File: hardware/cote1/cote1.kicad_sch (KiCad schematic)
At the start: 0 parts

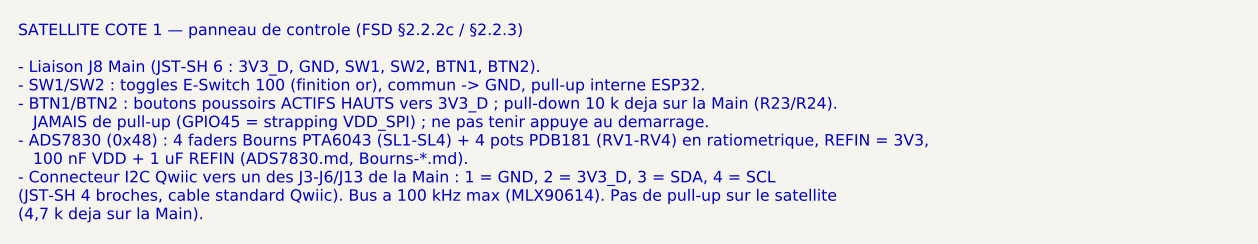
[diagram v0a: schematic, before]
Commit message: hardware+docs: CAP1298 retenu pour le tactile de Cote 2, BOM de reference corrigee (H8)
- Cote 2 : CAP1298-1-SL-TR (C2652072, 8 touches, 0x28 fixe) remplace le MTCH2120
  (aucun stock) ; proximite de Cote 3 en suspens (pas de second CAP12xx).
- BOM : U11 = LSM6DSOXTR, doublon U21 retire, filtre DAC 470 ohm + 2,2 nF C0G,
  TMAG5273A1 (C3716049), U10 SOT-23-6, ecran bouche a choisir, LCSC de D1/Q1/Q2
  dans la bonne colonne, ST25DV et haut-parleur ajoutes.
- docs/pcb/02-bom-lcsc.csv (perimee) supprimee : une seule BOM.
- FSD, RESTE-A-FAIRE, syntheses et cartouches satellites alignes.
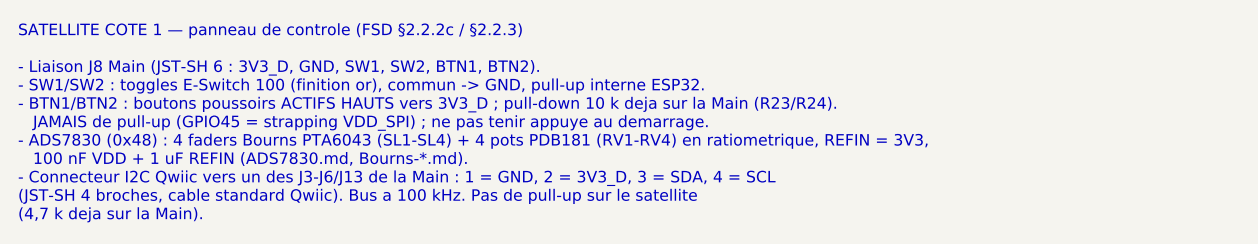
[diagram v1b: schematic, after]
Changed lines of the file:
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@@
 	(generator_version "10.0")
 	(paper "A4")
-	(text "SATELLITE COTE 1 — panneau de controle (FSD §2.2.2c / §2.2.3)\n\n- Liaison J8 Main (JST-SH 6 : 3V3_D, GND, SW1, SW2, BTN1, BTN2).\n- SW1/SW2 : toggles E-Switch 100 (finition or), commun -> GND, pull-up interne ESP32.\n- BTN1/BTN2 : boutons poussoirs ACTIFS HAUTS vers 3V3_D ; pull-down 10 k deja sur la Main (R23/R24).\n   JAMAIS de pull-up (GPIO45 = strapping VDD_SPI) ; ne pas tenir appuye au demarrage.\n- ADS7830 (0x48) : 4 faders Bourns PTA6043 (SL1-SL4) + 4 pots PDB181 (RV1-RV4) en ratiometrique, REFIN = 3V3,\n   100 nF VDD + 1 uF REFIN (ADS7830.md, Bourns-*.md).\n- Connecteur I2C Qwiic vers un des J3-J6/J13 de la Main : 1 = GND, 2 = 3V3_D, 3 = SDA, 4 = SCL\n(JST-SH 4 broches, cable standard Qwiic). Bus a 100 kHz max (MLX90614). Pas de pull-up sur le satellite\n(4,7 k deja sur la Main)."
+	(text "SATELLITE COTE 1 — panneau de controle (FSD §2.2.2c / §2.2.3)\n\n- Liaison J8 Main (JST-SH 6 : 3V3_D, GND, SW1, SW2, BTN1, BTN2).\n- SW1/SW2 : toggles E-Switch 100 (finition or), commun -> GND, pull-up interne ESP32.\n- BTN1/BTN2 : boutons poussoirs ACTIFS HAUTS vers 3V3_D ; pull-down 10 k deja sur la Main (R23/R24).\n   JAMAIS de pull-up (GPIO45 = strapping VDD_SPI) ; ne pas tenir appuye au demarrage.\n- ADS7830 (0x48) : 4 faders Bourns PTA6043 (SL1-SL4) + 4 pots PDB181 (RV1-RV4) en ratiometrique, REFIN = 3V3,\n   100 nF VDD + 1 uF REFIN (ADS7830.md, Bourns-*.md).\n- Connecteur I2C Qwiic vers un des J3-J6/J13 de la Main : 1 = GND, 2 = 3V3_D, 3 = SDA, 4 = SCL\n(JST-SH 4 broches, cable standard Qwiic). Bus a 100 kHz. Pas de pull-up sur le satellite\n(4,7 k deja sur la Main)."
 		(exclude_from_sim no)
 		(at 20.32 142.24 0)

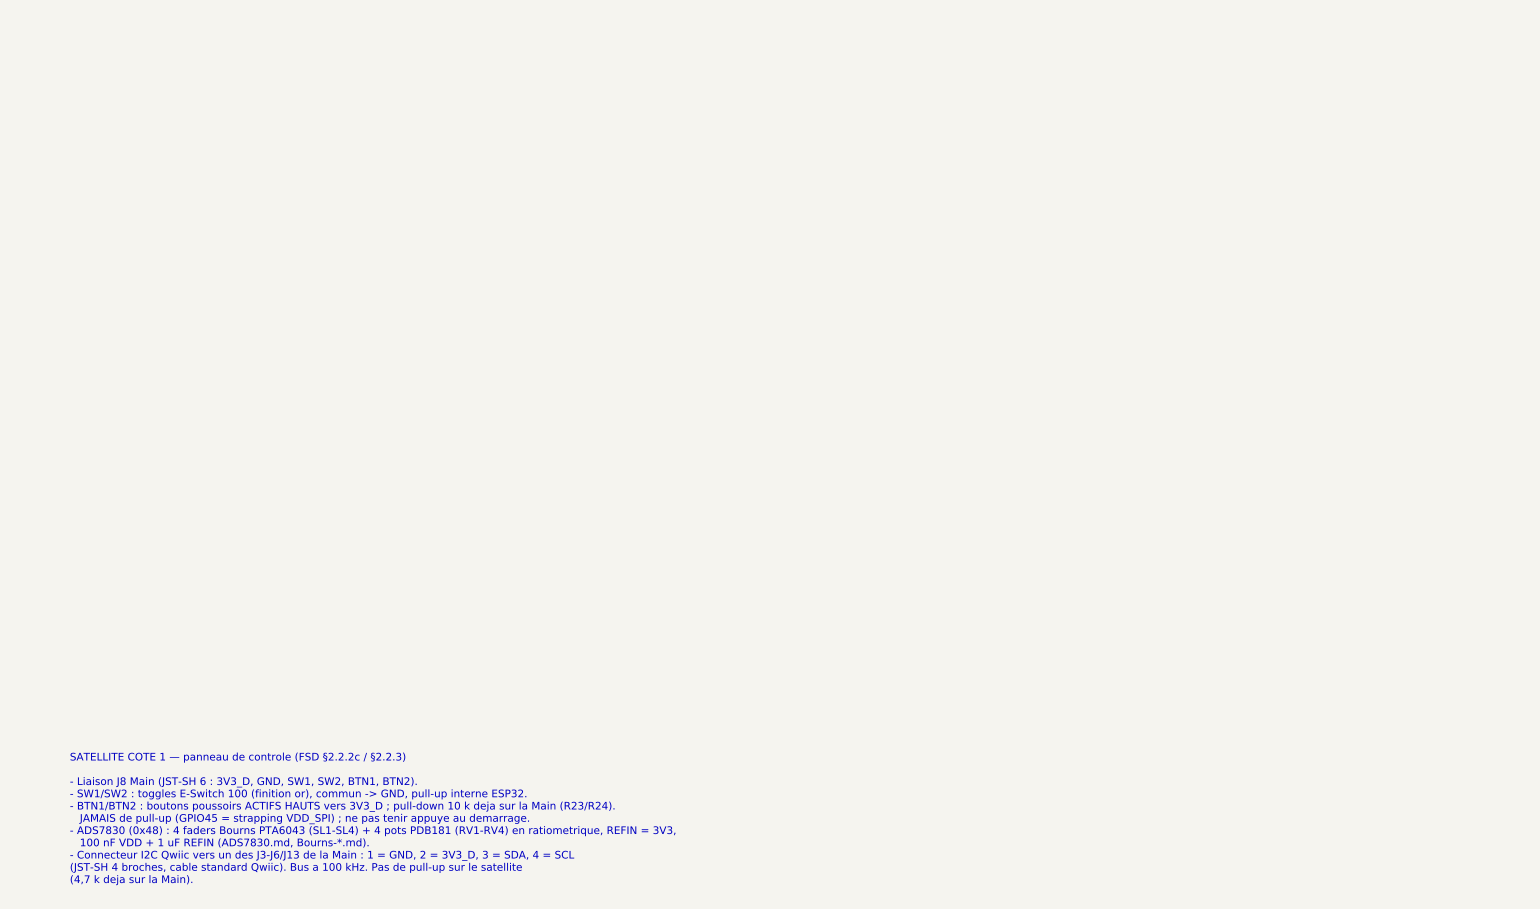
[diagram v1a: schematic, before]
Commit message: hardware: schemas des satellites Dessus, Devant, Cote 1 et Cote 3
- Dessus : ST25DV04KC (10 nF + 100 nF), antenne boucle ANT1 (~4,8 uH, empreinte a creer), accord C3 DNP, Qwiic
- Devant : BMP280 (CSB sur VDDIO, SDO GND), VEML7700, liaisons J7/J7b/J9, embases yeux/bouche provisoires, halo 8 WS2812B
- Cote 1 : ADS7830 ratiometrique, 4 faders PTA6043, 4 pots PDB181, liaison J8, toggles/boutons en facade sur JST-PH
- Cote 3 : TMAG5273A1 (INT et TEST a GND), 100 nF, Qwiic
- BOM : lignes satellites prefixees par face, recoupees avec les schemas
- Brochages corriges dans les syntheses : ST25DV (1 V_EH, 2 AC0) et VEML7700 (2 VDD, 4 SDA)
- Questions ouvertes : docs/audits/2026-09-27-questions-satellites.md
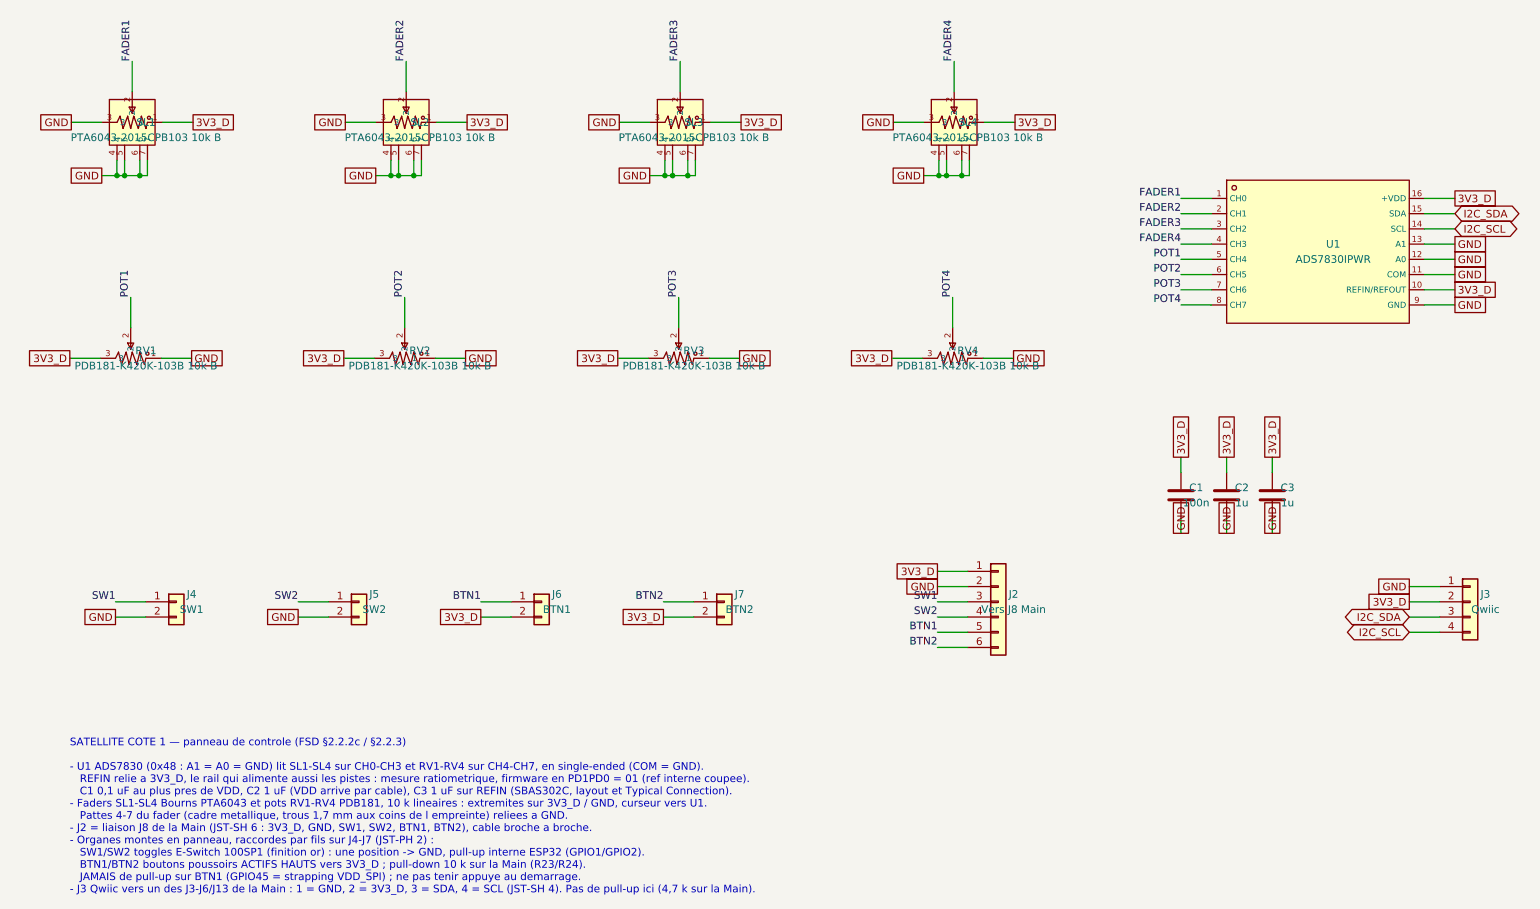
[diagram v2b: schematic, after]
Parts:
- added C1: 100n, Capacitor_SMD:C_0402_1005Metric, symbol Device:C
- added C2, C3: 1u, Capacitor_SMD:C_0402_1005Metric, symbol Device:C
- added J2: Vers J8 Main, Connector_JST:JST_SH_BM06B-SRSS-TB_1x06-1MP_P1.00mm_Vertical, symbol Connector_Generic:Conn_01x06
- added J3: Qwiic, Connector_JST:JST_SH_BM04B-SRSS-TB_1x04-1MP_P1.00mm_Vertical, symbol Connector_Generic:Conn_01x04
- added J4: SW1, Connector_JST:JST_PH_B2B-PH-K_1x02_P2.00mm_Vertical, symbol Connector_Generic:Conn_01x02
- added J5: SW2, Connector_JST:JST_PH_B2B-PH-K_1x02_P2.00mm_Vertical, symbol Connector_Generic:Conn_01x02
- added J6: BTN1, Connector_JST:JST_PH_B2B-PH-K_1x02_P2.00mm_Vertical, symbol Connector_Generic:Conn_01x02
- added J7: BTN2, Connector_JST:JST_PH_B2B-PH-K_1x02_P2.00mm_Vertical, symbol Connector_Generic:Conn_01x02
- added RV1, RV2, RV3, RV4: PDB181-K420K-103B 10k B, lcsc_footprints:C6251250_RES-ADJ-TH_PDB181-K420K-XXXB, symbol lcsc_imported:PDB181-K420K-103B
- added SL1, SL2, SL3, SL4: PTA6043-2015CPB103 10k B, lcsc_footprints:C17203852_RES-ADJ-TH_PTA6043-2015DPB103, symbol lcsc_imported:PTA6043-2015CPB103
- added U1: ADS7830IPWR, lcsc_footprints:C161747_TSSOP-16_L5_0-W4_4-P0_65-LS6_4-BL, symbol lcsc_imported:ADS7830IPWR
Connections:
- new net 3V3_D: C1.1, C2.1, C3.1, J2.1 (Pin_1), J3.2 (Pin_2), J6.2 (Pin_2), J7.2 (Pin_2), RV1.3, RV2.3, RV3.3, RV4.3, U1.10 (REFIN/REFOUT), U1.16 (+VDD)
- new net BTN1: J2.5 (Pin_5), J6.1 (Pin_1)
- new net BTN2: J2.6 (Pin_6), J7.1 (Pin_1)
- new net FADER1: U1.1 (CH0)
- new net FADER2: U1.2 (CH1)
- new net FADER3: U1.3 (CH2)
- new net FADER4: U1.4 (CH3)
- new net GND: C1.2, C2.2, C3.2, J2.2 (Pin_2), J3.1 (Pin_1), J4.2 (Pin_2), J5.2 (Pin_2), RV1.1, RV2.1, RV3.1, RV4.1, U1.11 (COM), U1.12 (A0), U1.13 (A1), U1.9 (GND)
- new net I2C_SCL: J3.4 (Pin_4), U1.14 (SCL)
- new net I2C_SDA: J3.3 (Pin_3), U1.15 (SDA)
- new net POT1: RV1.2, U1.5 (CH4)
- new net POT2: RV2.2, U1.6 (CH5)
- new net POT3: RV3.2, U1.7 (CH6)
- new net POT4: RV4.2, U1.8 (CH7)
- new net SW1: J2.3 (Pin_3), J4.1 (Pin_1)
- new net SW2: J2.4 (Pin_4), J5.1 (Pin_1)
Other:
- note added: "SATELLITE COTE 1 — panneau de controle (FSD §2.2.2c / §2.2.3) - U1 ADS7830 (0x48 : A1 = A0 = GND) lit SL1-SL4 sur CH0-CH3 et RV1-RV4 sur CH4-CH7, en single-ended (COM = GND). REFIN relie a 3V3_D, le rail qui alimente aussi les pistes : mesure ratiometrique, firmware en PD1PD0 = 01 (ref interne coupee). C1 0,1 uF au plus pres de VDD, C2 1 uF (VDD arrive par cable), C3 1 uF sur REFIN (SBAS302C, lay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"
- note removed: "SATELLITE COTE 1 — panneau de controle (FSD §2.2.2c / §2.2.3) - Liaison J8 Main (JST-SH 6 : 3V3_D, GND, SW1, SW2, BTN1, BTN2). - SW1/SW2 : toggles E-Switch 100 (finition or), commun -> GND, pull-up interne ESP32. - BTN1/BTN2 : boutons poussoirs ACTIFS HAUTS vers 3V3_D ; pull-down 10 k deja sur la Main (R23/R24). JAMAIS de pull-up (GPIO45 = strapping VDD_SPI) ; ne pas tenir appuye au demarrage. - 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"

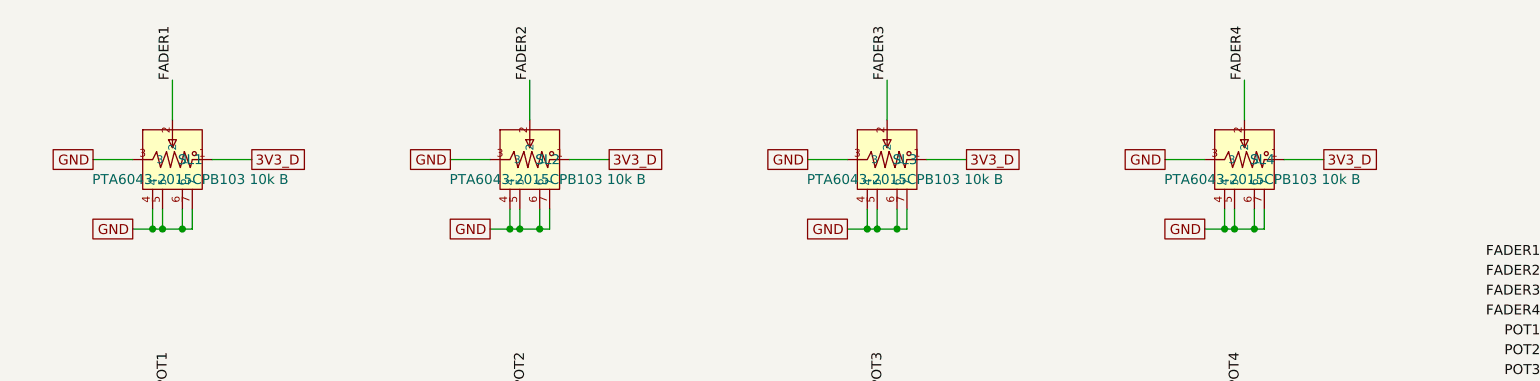
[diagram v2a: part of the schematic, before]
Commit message: hardware(satellites): fichiers Cote 3 / Devant rechargeables, faders de Cote 1 raccordes
- cartouches de Cote 3 et Devant : reste de l ancien texte colle apres le nouveau (guillemets
  echappes non geres par le script) -> erreur de chargement KiCad
- Cote 1 : extremites de fils arrondies au 1/100 mm alors que les pins du PTA6043 sont hors
  grille (5,334 mm...) -> 28 pins non connectees a l ERC ; coordonnees exactes
- cartouche de Devant remis sous le halo
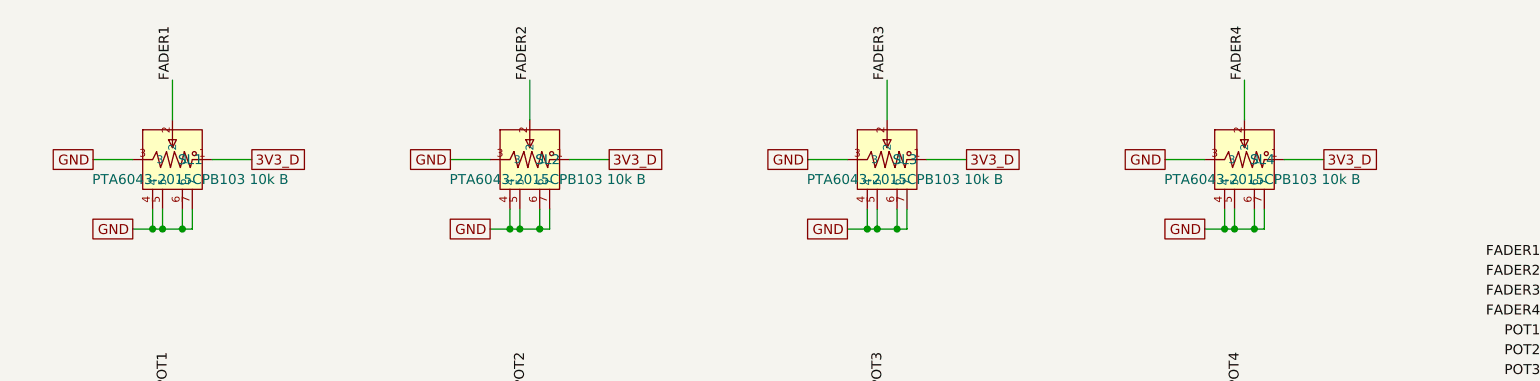
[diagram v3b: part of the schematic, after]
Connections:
- net 3V3_D: now also SL1.1, SL2.1, SL3.1, SL4.1
- net FADER1: now also SL1.2
- net FADER2: now also SL2.2
- net FADER3: now also SL3.2
- net FADER4: now also SL4.2
- net GND: now also SL1.3, SL1.4, SL1.5, SL1.6, SL1.7, SL2.3, SL2.4, SL2.5, SL2.6, SL2.7, SL3.3, SL3.4, SL3.5, SL3.6, SL3.7, SL4.3, SL4.4, SL4.5, SL4.6, SL4.7
